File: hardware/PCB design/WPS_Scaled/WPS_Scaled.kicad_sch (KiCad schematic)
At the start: 0 parts

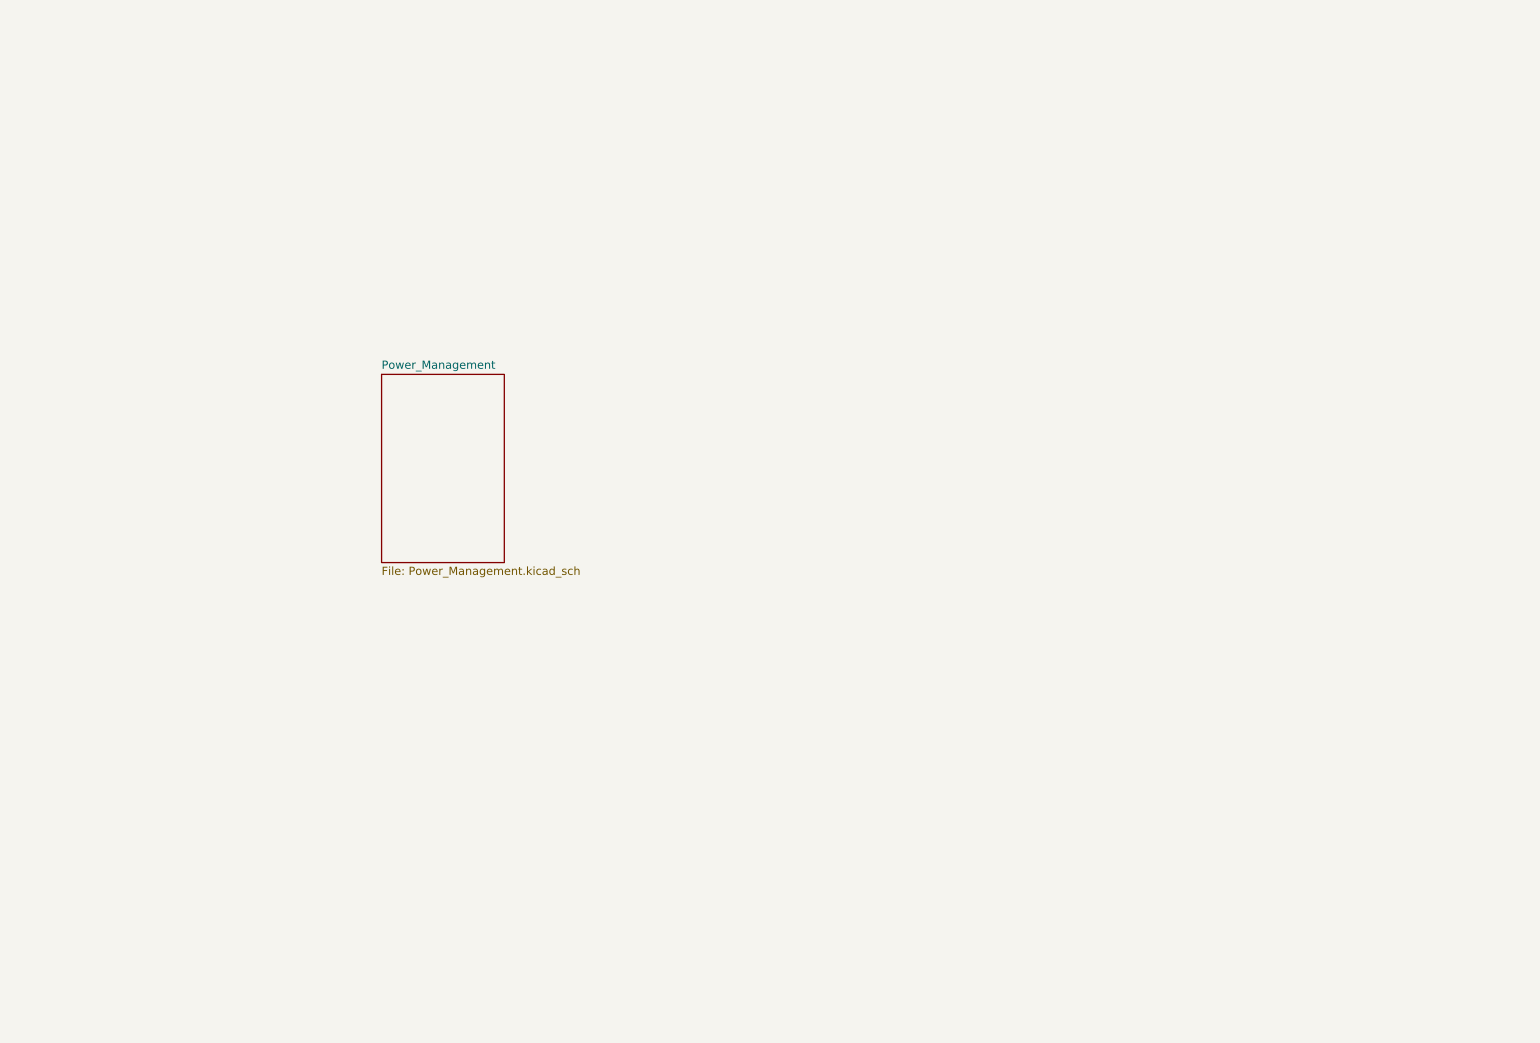
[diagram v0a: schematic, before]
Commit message: finalized with the sensors and actuator schematics
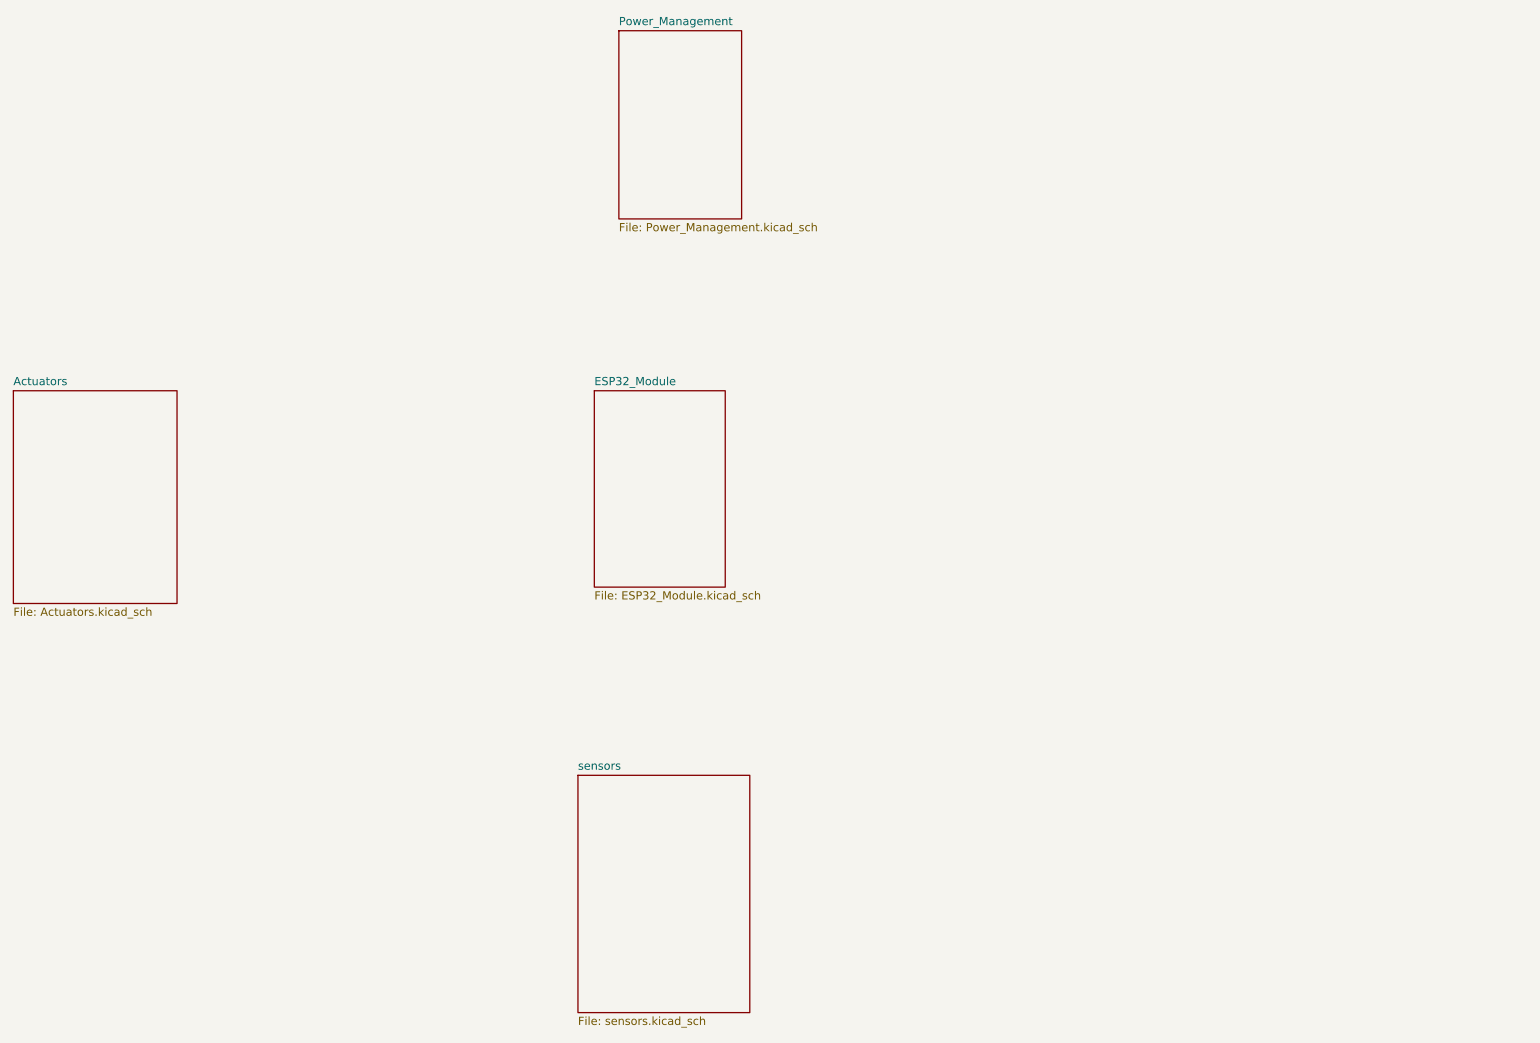
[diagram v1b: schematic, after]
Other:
- added sheet Actuators (Actuators.kicad_sch)
- added sheet ESP32_Module (ESP32_Module.kicad_sch)
- added sheet sensors (sensors.kicad_sch)
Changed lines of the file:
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@@
 	(paper "A4")
 	(sheet
-		(at 86.36 77.47)
+		(at 29.21 80.01)
+		(size 25.4 33.02)
+		(exclude_from_sim no)
+		(in_bom yes)
+		(on_board yes)
+		(dnp no)
+		(fields_autoplaced yes)
+		(stroke
+			(width 0.1524)
+			(type solid)
+		)
+		(fill
+			(color 255 201 7 1.0000)
+		)
+		(property "Sheetname" "Actuators"
+			(at 29.21 79.2984 0)
+			(effects
+				(font
+					(size 1.27 1.27)
+				)
+				(justify left bottom)
+			)
+		)
+		(property "Sheetfile" "Actuators.kicad_sch"
+			(at 29.21 113.6146 0)
+			(effects
+				(font
+					(size 1.27 1.27)
+				)
+				(justify left top)
+			)
+		)
+		(instances
+			(project "WPS_Scaled"
+				(path "/6ff23a5c-68c9-4176-a3db-3a9ab4454c0e"
+					(page "4")
+				)
+			)
+		)
+	)
+	(sheet
+		(at 123.19 24.13)
 		(size 19.05 29.21)
 		(exclude_from_sim no)
@@
 		)
 		(property "Sheetname" "Power_Management"
-			(at 86.36 76.7584 0)
+			(at 123.19 23.4184 0)
 			(effects
 				(font
@@
 		)
 		(property "Sheetfile" "Power_Management.kicad_sch"
-			(at 86.36 107.2646 0)
+			(at 123.19 53.9246 0)
 			(effects
 				(font
@@
 				)
 			)
+		)
+	)
+	(sheet
+		(at 116.84 139.7)
+		(size 26.67 36.83)
+		(exclude_from_sim no)
+		(in_bom yes)
+		(on_board yes)
+		(dnp no)
+		(fields_autoplaced yes)
+		(stroke
+			(width 0.1524)
+			(type solid)
+		)
+		(fill
+			(color 255 73 0 1.0000)
+		)
+		(property "Sheetname" "sensors"
+			(at 116.84 138.9884 0)
+			(effects
+				(font
+					(size 1.27 1.27)
+				)
+				(justify left bottom)
+			)
+		)
+		(property "Sheetfile" "sensors.kicad_sch"
+			(at 116.84 177.1146 0)
+			(effects
+				(font
+					(size 1.27 1.27)
+				)
+				(justify left top)
+			)
+		)
+		(instances
+			(project "WPS_Scaled"
+				(path "/6ff23a5c-68c9-4176-a3db-3a9ab4454c0e"
+					(page "5")
+				)
+			)
+		)
+	)
+	(sheet
+		(at 119.38 80.01)
+		(size 20.32 30.48)
+		(exclude_from_sim no)
+		(in_bom yes)
+		(on_board yes)
+		(dnp no)
+		(fields_autoplaced yes)
+		(stroke
+			(width 0.1524)
+			(type solid)
+		)
+		(fill
+			(color 116 255 0 1.0000)
+		)
+		(property "Sheetname" "ESP32_Module"
+			(at 119.38 79.2984 0)
+			(effects
+				(font
+					(size 1.27 1.27)
+				)
+				(justify left bottom)
+			)
+		)
+		(property "Sheetfile" "ESP32_Module.kicad_sch"
+			(at 119.38 111.0746 0)
+			(effects
+				(font
+					(size 1.27 1.27)
+				)
+				(justify left top)
+			)
+		)
+		(instances
+			(project "WPS_Scaled"
+				(path "/6ff23a5c-68c9-4176-a3db-3a9ab4454c0e"
+					(page "3")
+				)
+			)

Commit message: finalized the pcb schematics
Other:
- added sheet User_Interface (User_Interface.kicad_sch)
- sheet Actuators ports: added ACTUATOR_PUMP_EN, ACTUATOR_UV_EN, ACTUATOR_VALVE_EN; removed none
- sheet ESP32_Module ports: added ACTUATOR_PUMP_EN, ACTUATOR_UV_EN, ACTUATOR_VALVE_EN, BUTTON_SYSTEM_RESET, DISPLAY_SCL, DISPLAY_SDA, LED_MAINTENANCE, LED_POWER_ON, SENSOR_COLOR_SCL, SENSOR_COLOR_SDA, SENSOR_CURRENT_SCL, SENSOR_CURRENT_SDA, SENSOR_FLOW_SIGNAL, SENSOR_LEVEL_ECHO, SENSOR_LEVEL_TRIG, SENSOR_PH_SIGNAL, SENSOR_PRESSURE_SIGNAL, SENSOR_TDS_SIGNAL, SENSOR_TURBIDITY_SIGNAL, SWITCHED_5V_EN; removed none
- sheet Power_Management ports: added SENSOR_CURRENT_N, SENSOR_CURRENT_P, SWITCHED_5V_EN; removed none
- sheet sensors ports: added SENSOR_COLOR_SCL, SENSOR_COLOR_SDA, SENSOR_CURRENT_N, SENSOR_CURRENT_P, SENSOR_CURRENT_SCL, SENSOR_CURRENT_SDA, SENSOR_FLOW_SIGNAL, SENSOR_LEVEL_ECHO, SENSOR_LEVEL_TRIG, SENSOR_PH_SIGNAL, SENSOR_PRESSURE_SIGNAL, SENSOR_TDS_SIGNAL, SENSOR_TURBIDITY_SIGNAL; removed none
- company: (none) -> Makerere University
- title: (none) -> Power Management

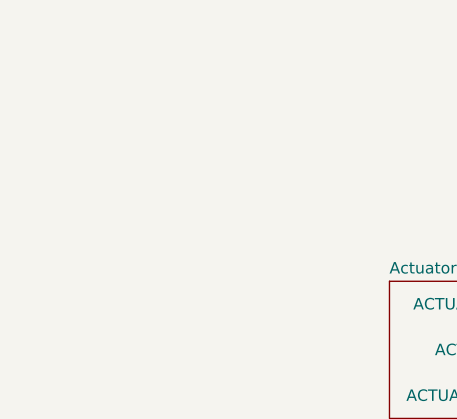
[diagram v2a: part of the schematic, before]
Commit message: updated the pcb component placements
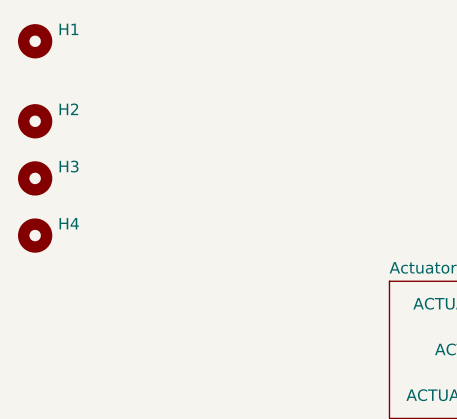
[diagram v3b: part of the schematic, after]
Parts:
- added H1, H2, H3, H4: MountingHole, MountingHole:MountingHole_3.2mm_M3, symbol Mechanical:MountingHole
